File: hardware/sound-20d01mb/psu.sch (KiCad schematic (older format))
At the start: 13 parts

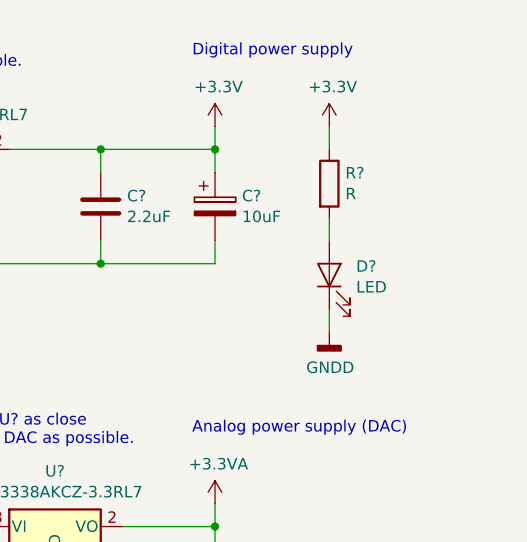
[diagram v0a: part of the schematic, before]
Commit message: Added X977B04
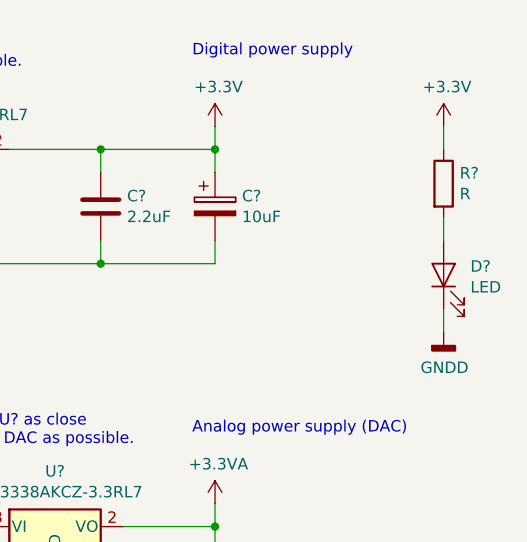
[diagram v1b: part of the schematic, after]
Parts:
- C?: footprint (none) -> Capacitor_SMD:CP_Elec_6.3x5.4
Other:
- moved on the sheet: D?, R?
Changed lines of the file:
@@
 F 0 "C?" H 3568 3096 50  0000 L CNN
 F 1 "47uF" H 3568 3005 50  0000 L CNN
-F 2 "" H 3488 2900 50  0001 C CNN
+F 2 "Capacitor_SMD:CP_Elec_6.3x5.4" H 3488 2900 50  0001 C CNN
 F 3 "~" H 3450 3050 50  0001 C CNN
 	1    3450 3050
@@
 L Device:LED D?
 U 1 1 61475539
-P 7350 3350
-F 0 "D?" V 7388 3233 50  0000 R CNN
-F 1 "LED" V 7297 3233 50  0000 R CNN
-F 2 "LED_SMD:LED_1206_3216Metric_Pad1.42x1.75mm_HandSolder" H 7350 3350 50  0001 C CNN
-F 3 "~" H 7350 3350 50  0001 C CNN
-	1    7350 3350
+P 7850 3350
+F 0 "D?" V 7888 3233 50  0000 R CNN
+F 1 "LED" V 7797 3233 50  0000 R CNN
+F 2 "LED_SMD:LED_1206_3216Metric_Pad1.42x1.75mm_HandSolder" H 7850 3350 50  0001 C CNN
+F 3 "~" H 7850 3350 50  0001 C CNN
+	1    7850 3350
 	0    -1   -1   0
 $EndComp
 Wire Wire Line
-	7350 3200 7350 3100
+	7850 3200 7850 3100
 Wire Wire Line
-	7350 2800 7350 2700
+	7850 2800 7850 2700
 $Comp
 L power:+3.3V #PWR?
 U 1 1 61475F89
-P 7350 2700
-F 0 "#PWR?" H 7350 2550 50  0001 C CNN
-F 1 "+3.3V" H 7365 2873 50  0000 C CNN
-F 2 "" H 7350 2700 50  0001 C CNN
-F 3 "" H 7350 2700 50  0001 C CNN
-	1    7350 2700
+P 7850 2700
+F 0 "#PWR?" H 7850 2550 50  0001 C CNN
+F 1 "+3.3V" H 7865 2873 50  0000 C CNN
+F 2 "" H 7850 2700 50  0001 C CNN
+F 3 "" H 7850 2700 50  0001 C CNN
+	1    7850 2700
 	1    0    0    -1
 $EndComp
@@
 L Device:R R?
 U 1 1 61476045
-P 7350 2950
-F 0 "R?" H 7420 2996 50  0000 L CNN
-F 1 "R" H 7420 2905 50  0000 L CNN
-F 2 "Resistor_SMD:R_1206_3216Metric_Pad1.42x1.75mm_HandSolder" V 7280 2950 50  0001 C CNN
-F 3 "~" H 7350 2950 50  0001 C CNN
-	1    7350 2950
+P 7850 2950
+F 0 "R?" H 7920 2996 50  0000 L CNN
+F 1 "R" H 7920 2905 50  0000 L CNN
+F 2 "Resistor_SMD:R_1206_3216Metric_Pad1.42x1.75mm_HandSolder" V 7780 2950 50  0001 C CNN
+F 3 "~" H 7850 2950 50  0001 C CNN
+	1    7850 2950
 	1    0    0    -1
 $EndComp
@@
 L power:GNDD #PWR?
 U 1 1 614762B1
-P 7350 3600
-F 0 "#PWR?" H 7350 3350 50  0001 C CNN
-F 1 "GNDD" H 7354 3445 50  0000 C CNN
-F 2 "" H 7350 3600 50  0001 C CNN
-F 3 "" H 7350 3600 50  0001 C CNN
-	1    7350 3600
+P 7850 3600
+F 0 "#PWR?" H 7850 3350 50  0001 C CNN
+F 1 "GNDD" H 7854 3445 50  0000 C CNN
+F 2 "" H 7850 3600 50  0001 C CNN
+F 3 "" H 7850 3600 50  0001 C CNN
+	1    7850 3600
 	1    0    0    -1
 $EndComp
 Wire Wire Line
-	7350 3500 7350 3600
+	7850 3500 7850 3600
 Wire Wire Line
 	5950 2800 6350 2800

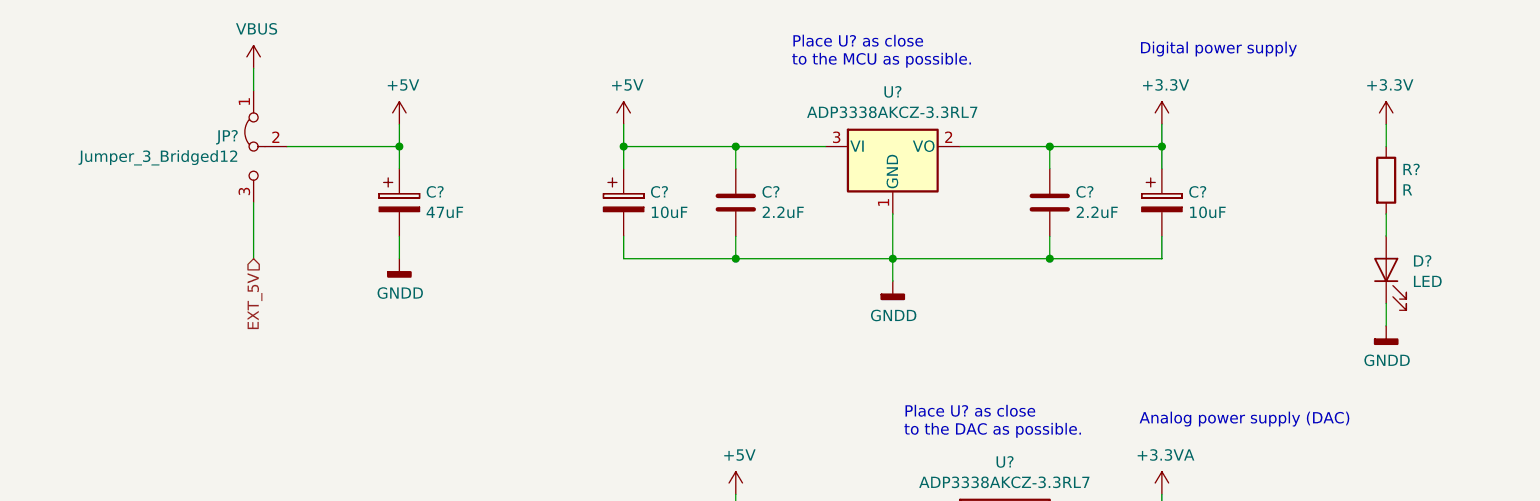
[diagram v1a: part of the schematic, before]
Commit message: Added fuse for USB
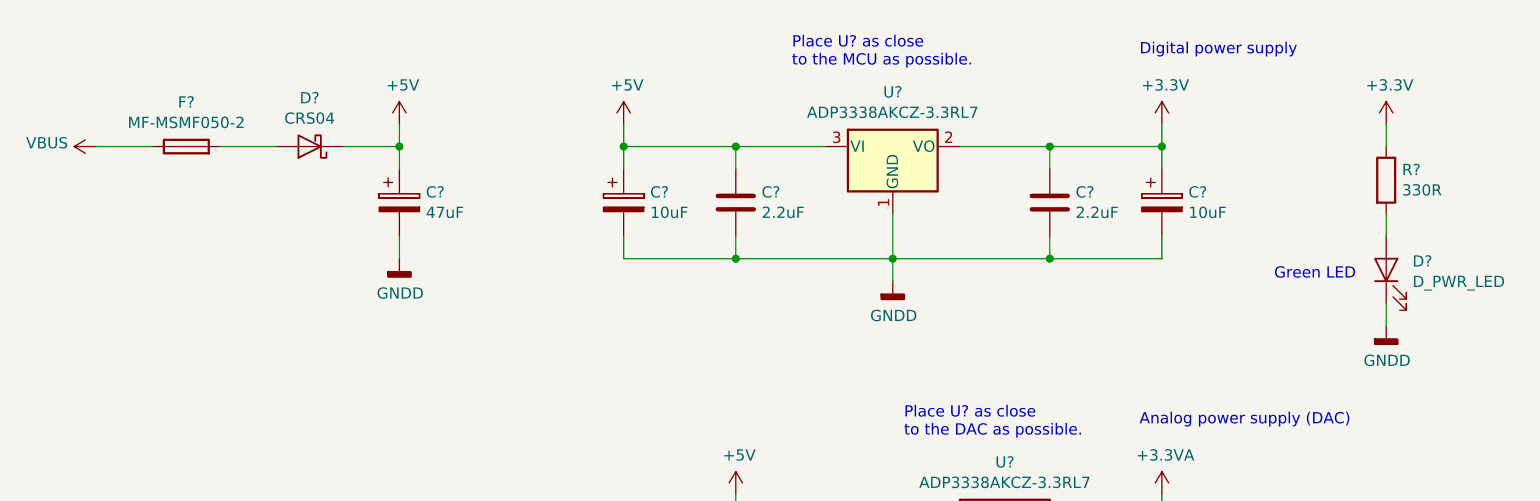
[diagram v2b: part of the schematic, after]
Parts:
- removed JP?: Jumper_3_Bridged12, Connector_PinHeader_2.54mm:PinHeader_1x03_P2.54mm_Vertical, symbol Jumper:Jumper_3_Bridged12
- added D?: CRS04, Diode_SMD:D_SOD-123F, symbol Device:D_Schottky
- added F?: MF-MSMF050-2, symbol Device:Fuse
- D?: value LED -> D_PWR_LED
- R?: value R -> 330R
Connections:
- net +5V: now also D?.1 (K)
- net VBUS: now also F?.1
- new net: D?.2 (A), F?.2
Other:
- note added: "Green LED"
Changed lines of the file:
@@
-$EndComp
-$Comp
-L power:VBUS #PWR?
-U 1 1 60E9D839
-P 2800 2450
-F 0 "#PWR?" H 2800 2300 50  0001 C CNN
-F 1 "VBUS" H 2815 2623 50  0000 C CNN
-F 2 "" H 2800 2450 50  0001 C CNN
-F 3 "" H 2800 2450 50  0001 C CNN
-	1    2800 2450
-	1    0    0    -1
 $EndComp
 $Comp
@@
 	1    0    0    -1
 $EndComp
-Text HLabel 2800 3300 3    50   Input ~ 0
-EXT_5V
-$Comp
-L Jumper:Jumper_3_Bridged12 JP?
-U 1 1 60E9DBAE
-P 2800 2800
-F 0 "JP?" V 2754 2866 50  0000 L CNN
-F 1 "Jumper_3_Bridged12" V 2845 2866 50  0000 L CNN
-F 2 "Connector_PinHeader_2.54mm:PinHeader_1x03_P2.54mm_Vertical" H 2800 2800 50  0001 C CNN
-F 3 "~" H 2800 2800 50  0001 C CNN
-	1    2800 2800
-	0    -1   1    0
-$EndComp
-Wire Wire Line
-	2800 2550 2800 2450
 $Comp
 L Device:CP C?
@@
 	1    0    0    -1
 $EndComp
-Wire Wire Line
-	2950 2800 3450 2800
-Wire Wire Line
-	3450 2800 3450 2900
 $Comp
 L power:GNDD #PWR?
@@
 Wire Wire Line
 	6850 3300 6350 3300
-Wire Wire Line
-	2800 3050 2800 3300
 Text Notes 5200 2450 0    50   ~ 0
 Place U? as close\nto the MCU as possible.
@@
 P 7850 3350
 F 0 "D?" V 7888 3233 50  0000 R CNN
-F 1 "LED" V 7797 3233 50  0000 R CNN
+F 1 "D_PWR_LED" V 7797 3233 50  0000 R CNN
 F 2 "LED_SMD:LED_1206_3216Metric_Pad1.42x1.75mm_HandSolder" H 7850 3350 50  0001 C CNN
 F 3 "~" H 7850 3350 50  0001 C CNN
@@
 P 7850 2950
 F 0 "R?" H 7920 2996 50  0000 L CNN
-F 1 "R" H 7920 2905 50  0000 L CNN
+F 1 "330R" H 7920 2905 50  0000 L CNN
 F 2 "Resistor_SMD:R_1206_3216Metric_Pad1.42x1.75mm_HandSolder" V 7780 2950 50  0001 C CNN
 F 3 "~" H 7850 2950 50  0001 C CNN
@@
 	4450 2800 4450 2700
 Connection ~ 4450 2800
+$Comp
+L Device:D_Schottky D?
+U 1 1 615390F1
+P 3050 2800
+F 0 "D?" H 3050 2584 50  0000 C CNN
+F 1 "CRS04" H 3050 2675 50  0000 C CNN
+F 2 "Diode_SMD:D_SOD-123F" H 3050 2800 50  0001 C CNN
+F 3 "~" H 3050 2800 50  0001 C CNN
+	1    3050 2800
+	-1   0    0    1
+$EndComp
+Text Notes 7350 3400 0    50   ~ 0
+Green LED
+$Comp
+L power:VBUS #PWR?
+U 1 1 6156F801
+P 2100 2800
+F 0 "#PWR?" H 2100 2650 50  0001 C CNN
+F 1 "VBUS" V 2115 2927 50  0000 L CNN
+F 2 "" H 2100 2800 50  0001 C CNN
+F 3 "" H 2100 2800 50  0001 C CNN
+	1    2100 2800
+	0    -1   -1   0
+$EndComp
+$Comp
+L Device:Fuse F?
+U 1 1 6157C2E8
+P 2500 2800
+F 0 "F?" V 2697 2800 50  0000 C CNN
+F 1 "MF-MSMF050-2" V 2606 2800 50  0000 C CNN
+F 2 "" V 2430 2800 50  0001 C CNN
+F 3 "~" H 2500 2800 50  0001 C CNN
+	1    2500 2800
+	0    -1   -1   0
+$EndComp
+Wire Wire Line
+	3450 2800 3200 2800
 Wire Wire Line
 	3450 2700 3450 2800
 Connection ~ 3450 2800
+Wire Wire Line
+	3450 2800 3450 2900
+Wire Wire Line
+	2900 2800 2650 2800
+Wire Wire Line
+	2350 2800 2100 2800
 $EndSCHEMATC
